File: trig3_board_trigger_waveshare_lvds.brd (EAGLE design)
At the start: 233.2 x 160 mm, 132 parts, among them IC1 SN65LVDT388ADBT, IC2 SN65LVDT388ADBT, IC3 SN65LVDT388ADBT, IC4 SN65LVDT388ADBT, IC5 SN65LVDT388ADBT, IC6 SN65LVDT388ADBT, IC7 SN65LVDT388ADBT, IC8 SN65LVDT388ADBT, J1 8pin, J10 8pin, J11 8pin, J12 4p-2.54, J13 8pin, J14 8pin, J15 8pin, J16 8pin, J17 8pin, J19 6HE-160-VG64AC, J2 8pin, J20 8pin, J3 4p-2.54, J4 4p-2.54, J5 8pin, J6 8pin, J7 8pin, J8 8pin, J9 8pin, X1 87758-1616, X13 87758-2816, X14 87758-2816, X15 87758-1616, X16 87758-1616, X17 87758-2816, X18 87758-2816, X2 87758-1616

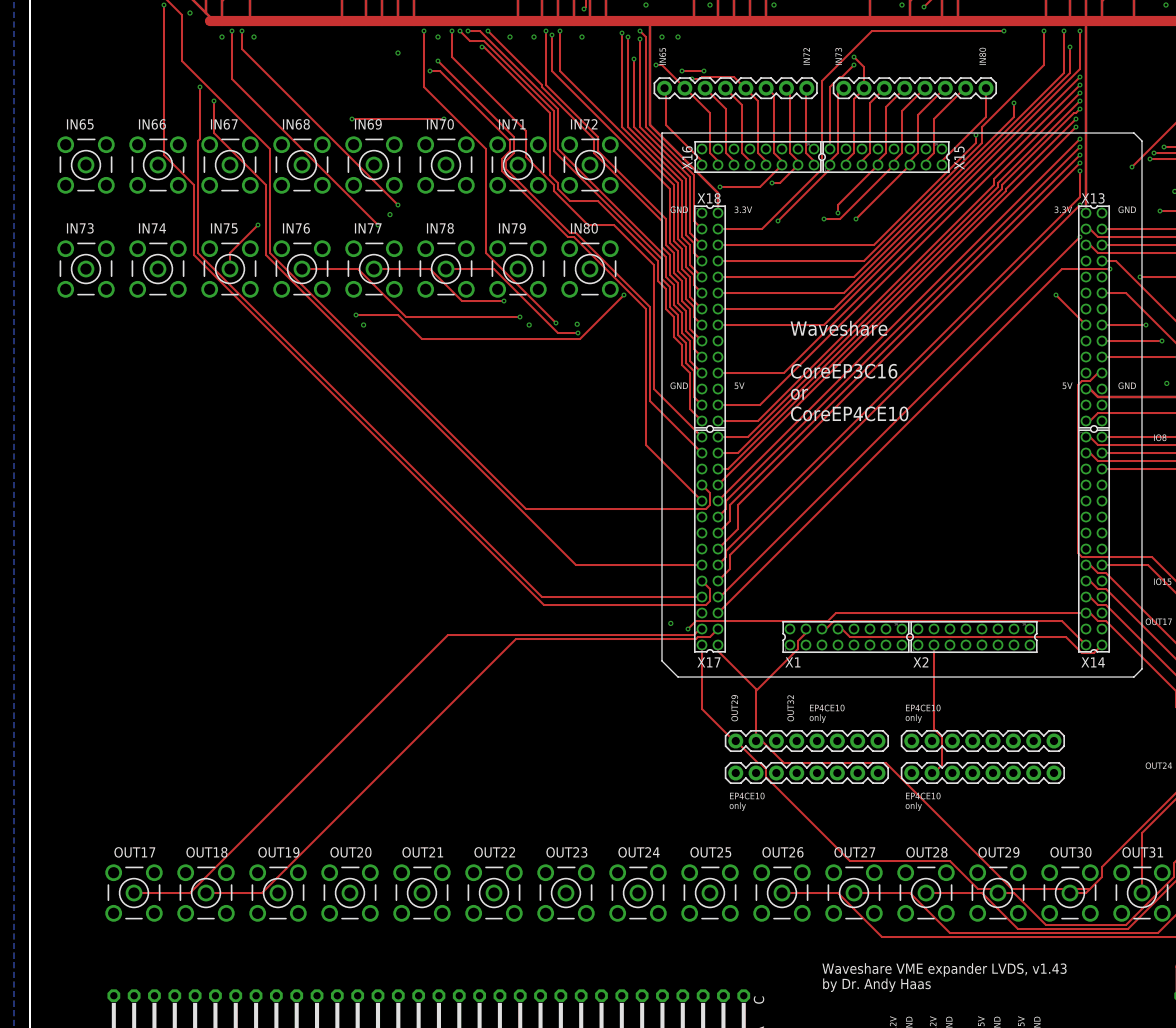
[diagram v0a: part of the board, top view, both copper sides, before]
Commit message: added 50 ohm term on extra sma inputs, v1.44
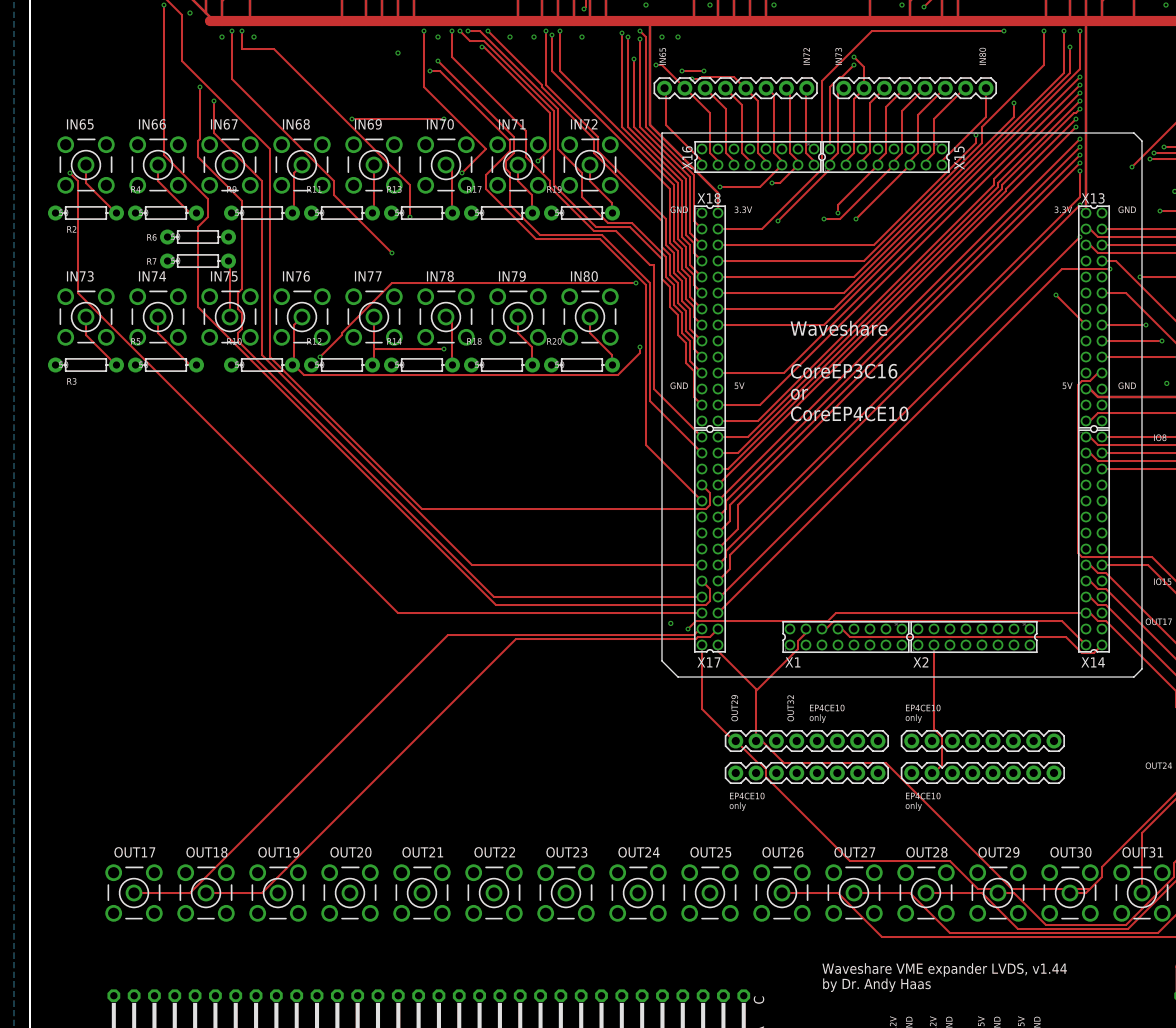
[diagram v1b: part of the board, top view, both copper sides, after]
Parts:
- added R10, R11, R12, R13, R14, R17, R18, R19, R2, R20, R3, R4, R5, R6, R7, R9: 50, SparkFun-Resistors:AXIAL-0.3
- moved IN73 6.00 mm to (-43.0, 45.0)
- moved IN74 6.00 mm to (-34.0, 45.0)
- moved IN75 6.00 mm to (-25.0, 45.0)
- moved IN76 6.00 mm to (-16.0, 45.0)
- moved IN77 6.00 mm to (-7.00, 45.0)
- moved IN78 6.00 mm to (2.00, 45.0)
- moved IN79 6.00 mm to (11.0, 45.0)
- moved IN80 6.00 mm to (20.0, 45.0)
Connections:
- net GND: now also R10.P$1, R11.P$1, R12.P$1, R13.P$1, R14.P$1, R17.P$1, R18.P$1, R19.P$1, R2.P$1, R20.P$1, R3.P$1, R4.P$1, R5.P$1, R6.P$1, R7.P$1, R9.P$1
- net IN65: now also R2.P$2
- net IN66: now also R4.P$2
- net IN67: now also R6.P$2
- net IN68: now also R9.P$2
- net IN69: now also R11.P$2
- net IN70: now also R13.P$2
- net IN71: now also R17.P$2
- net IN72: now also R19.P$2
- net IN73: now also R3.P$2
- net IN74: now also R5.P$2
- net IN75: now also R7.P$2
- net IN76: now also R10.P$2
- net IN77: now also R12.P$2
- net IN78: now also R14.P$2
- net IN79: now also R18.P$2
- net IN80: now also R20.P$2
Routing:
- net IN13: track 76.5 -> 104.9 mm, vias 2 -> 3
- net IN10: track 79.0 -> 98.5 mm
- net IN74: track 157.0 -> 169.7 mm
- net IN7: track 91.9 -> 103.7 mm
- net IN80: track 61.3 -> 72.1 mm
- net IN79: track 83.1 -> 93.8 mm
- net IN67: track 77.4 -> 87.2 mm
- net IN76: track 93.9 -> 103.0 mm
- net IN66: track 83.6 -> 92.0 mm
- net IN1: track 136.2 -> 144.5 mm, vias 1 -> 2
- net IN9: track 142.3 -> 149.9 mm
- net IN4: track 108.6 -> 116.2 mm
- net IN65: track 87.9 -> 95.5 mm
- net IN6: track 95.7 -> 102.7 mm
- net IN77: track 84.9 -> 91.9 mm
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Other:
- board text added: "Waveshare VME expander LVDS, v1.44 by Dr. Andy Haas"
- board text removed: "Waveshare VME expander LVDS, v1.43 by Dr. Andy Haas"
